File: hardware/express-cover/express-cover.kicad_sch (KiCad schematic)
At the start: 26 parts

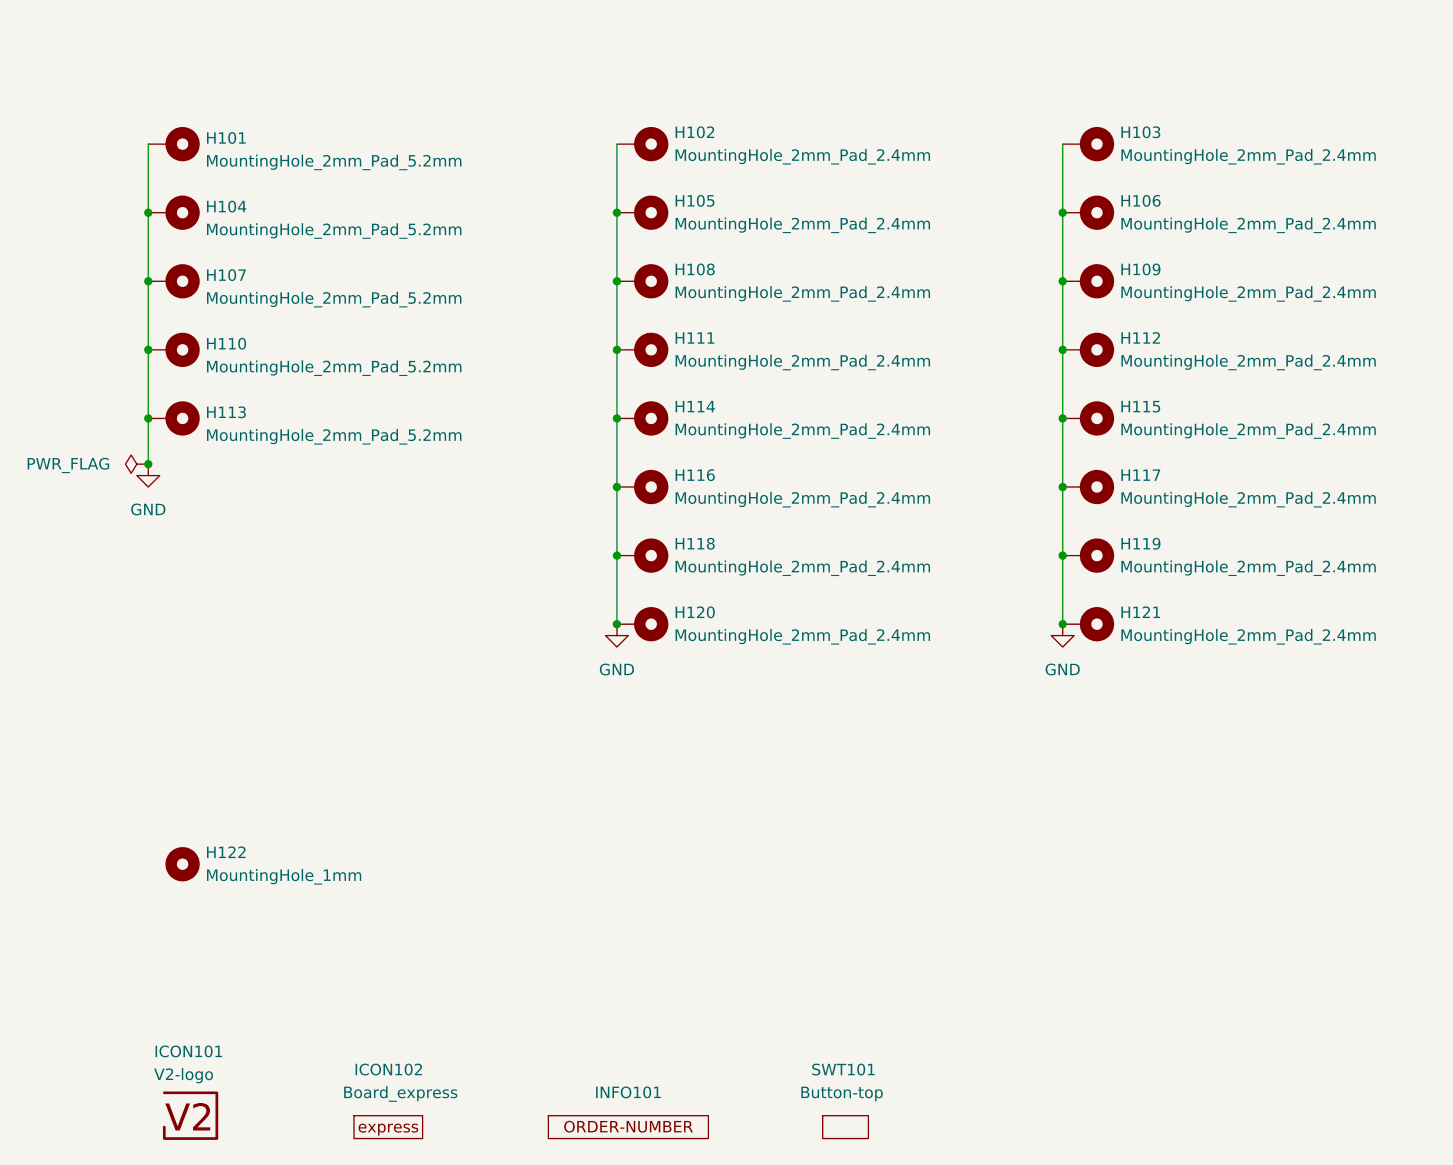
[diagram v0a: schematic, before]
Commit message: Replace Order_Number
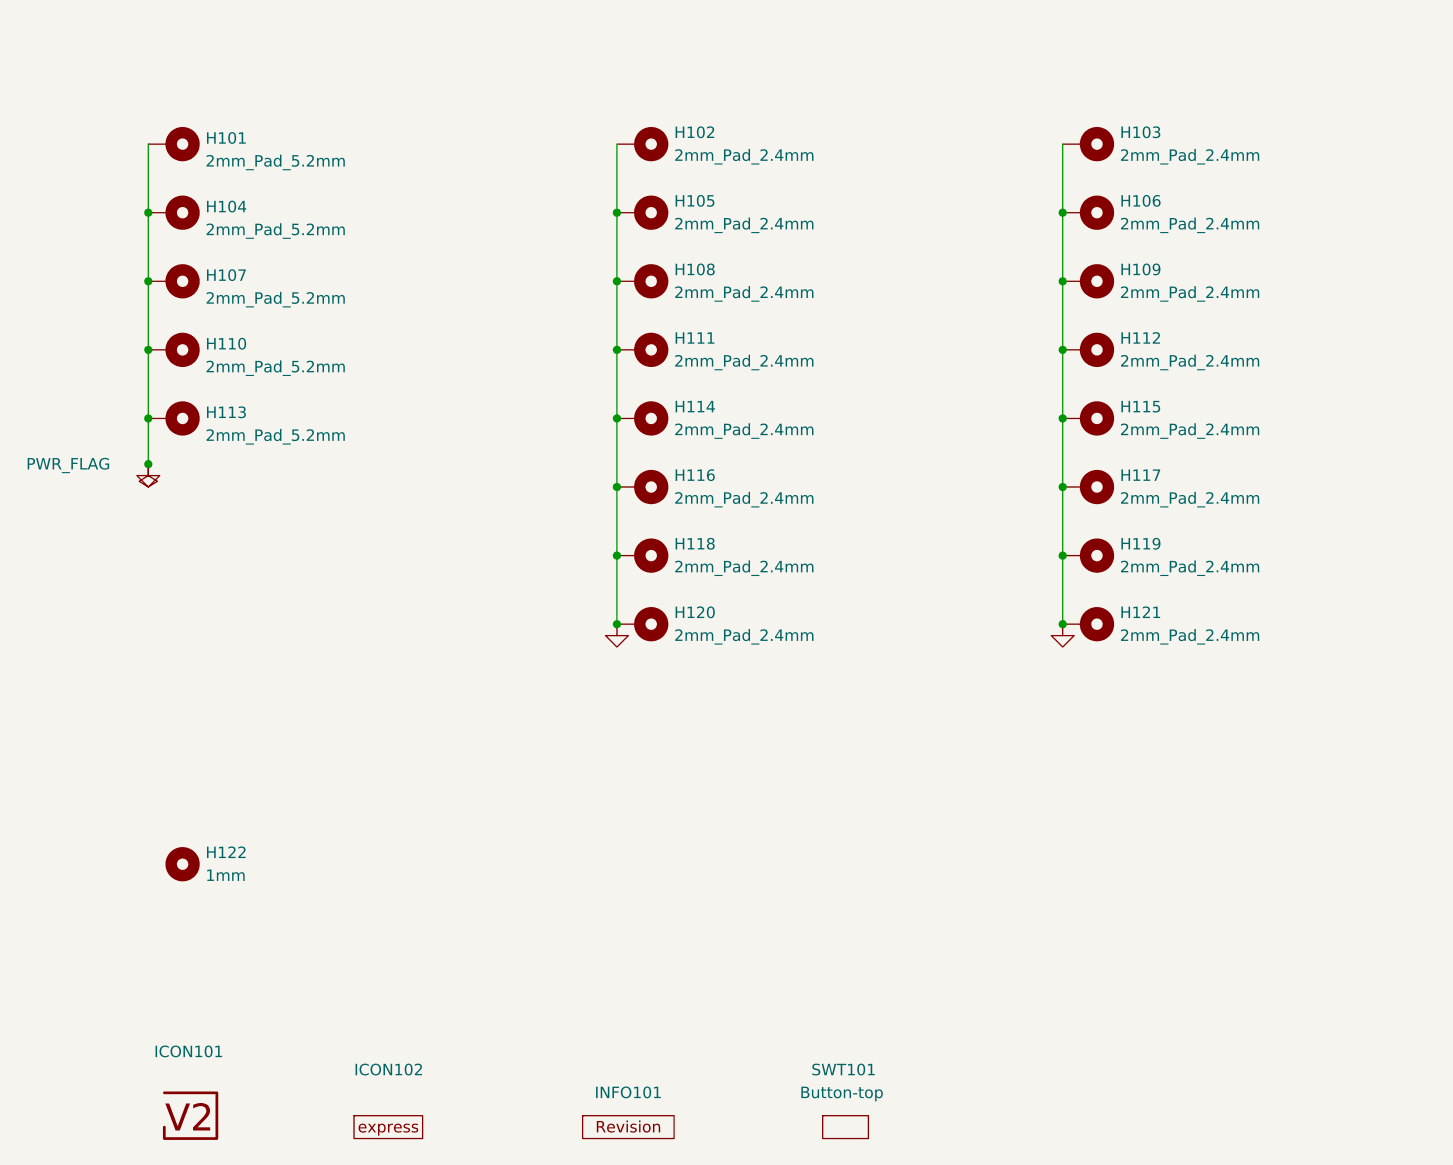
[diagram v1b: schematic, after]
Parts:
- H101, H104, H107, H110, H113: value MountingHole_2mm_Pad_5.2mm -> 2mm_Pad_5.2mm
- H102, H103, H105, H106, H108, H109, H111, H112, H114, H115, H116, H117, H118, H119, H120, H121: value MountingHole_2mm_Pad_2.4mm -> 2mm_Pad_2.4mm
- H122: value MountingHole_1mm -> 1mm
- INFO101: value Order_Number -> ~; footprint V2_Production:Order_Number -> V2_Production:Revision; symbol V2_Production:Order_Number -> V2_Production:Revision

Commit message: Update Library
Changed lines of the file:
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@@
-	)
-	(junction
-		(at 82.55 78.74)
-		(diameter 0)
-		(color 0 0 0 0)
 	)
 	(junction
@@
 		(dnp no)
 		(fields_autoplaced yes)
-		(property "Reference" "#PWR0103"
+		(property "Reference" "#PWR103"
 			(at 184.15 102.87 0)
 			(effects
@@
 			(project "express-cover"
 				(path "/6c8448b4-b04d-47e1-934e-e40cbe27a7be"
-					(reference "#PWR0103")
+					(reference "#PWR103")
 					(unit 1)
 				)
@@
 		(dnp no)
 		(fields_autoplaced yes)
-		(property "Reference" "#PWR0101"
+		(property "Reference" "#PWR101"
 			(at 82.55 85.09 0)
 			(effects
@@
 			(project "express-cover"
 				(path "/6c8448b4-b04d-47e1-934e-e40cbe27a7be"
-					(reference "#PWR0101")
+					(reference "#PWR101")
 					(unit 1)
 				)
@@
 	)
 	(symbol
+		(lib_id "V2_power:GND")
+		(at 86.36 30.48 90)
+		(unit 1)
+		(exclude_from_sim no)
+		(in_bom yes)
+		(on_board yes)
+		(dnp no)
+		(fields_autoplaced yes)
+		(property "Reference" "#PWR0104"
+			(at 92.71 30.48 0)
+			(effects
+				(font
+					(size 1.27 1.27)
+				)
+				(hide yes)
+			)
+		)
+		(property "Value" "GND"
+			(at 91.44 30.48 0)
+			(effects
+				(font
+					(size 1.27 1.27)
+				)
+				(hide yes)
+			)
+		)
+		(property "Footprint" ""
+			(at 86.36 30.48 0)
+			(effects
+				(font
+					(size 1.27 1.27)
+				)
+				(hide yes)
+			)
+		)
+		(property "Datasheet" ""
+			(at 86.36 30.48 0)
+			(effects
+				(font
+					(size 1.27 1.27)
+				)
+				(hide yes)
+			)
+		)
+		(property "Description" ""
+			(at 86.36 30.48 0)
+			(effects
+				(font
+					(size 1.27 1.27)
+				)
+				(hide yes)
+			)
+		)
+		(pin "1"
+		)
+		(instances
+			(project "express-cover"
+				(path "/6c8448b4-b04d-47e1-934e-e40cbe27a7be"
+					(reference "#PWR0104")
+					(unit 1)
+				)
+			)
+		)
+	)
+	(symbol
 		(lib_id "V2_Mechanical:MountingHole_2mm_Pad_2.4mm")
 		(at 137.16 43.18 270)
@@
 		(dnp no)
 		(fields_autoplaced yes)
-		(property "Reference" "#PWR0102"
+		(property "Reference" "#PWR102"
 			(at 134.62 102.87 0)
 			(effects
@@
 			(project "express-cover"
 				(path "/6c8448b4-b04d-47e1-934e-e40cbe27a7be"
-					(reference "#PWR0102")
+					(reference "#PWR102")
 					(unit 1)
 				)
@@
 	(symbol
 		(lib_id "V2_power:PWR_FLAG")
-		(at 82.55 78.74 90)
+		(at 86.36 30.48 0)
 		(unit 1)
 		(exclude_from_sim no)
@@
 		(on_board yes)
 		(dnp no)
-		(property "Reference" "#FLG0101"
-			(at 80.645 78.74 0)
+		(property "Reference" "#FLG101"
+			(at 86.36 28.575 0)
 			(effects
 				(font
@@
 		)
 		(property "Value" "PWR_FLAG"
-			(at 73.66 78.74 90)
+			(at 74.93 30.48 0)
 			(effects
 				(font
@@
 		)
 		(property "Footprint" ""
-			(at 82.55 78.74 0)
-			(effects
-				(font
-					(size 1.27 1.27)
-				)
-				(hide yes)
-			)
-		)
-		(property "Datasheet" ""
-			(at 82.55 78.74 0)
+			(at 86.36 30.48 0)
+			(effects
+				(font
+					(size 1.27 1.27)
+				)
+				(hide yes)
+			)
+		)
+		(property "Datasheet" ""
+			(at 86.36 30.48 0)
 			(effects
 				(font
@@
 		)
 		(property "Description" "Special symbol for telling ERC where power comes from"
-			(at 82.55 78.74 0)
-			(effects
-				(font
-					(size 1.27 1.27)
-				)
-				(hide yes)
-			)
-		)
-		(pin "1"
-		)
-		(instances
-			(project "express-cover"
-				(path "/6c8448b4-b04d-47e1-934e-e40cbe27a7be"
-					(reference "#FLG0101")
-					(unit 1)
-				)
+			(at 86.36 30.48 0)
+			(effects
+				(font
+					(size 1.27 1.27)
+				)
+				(hide yes)
+			)
+		)
+		(pin "1"
+		)
+		(instances
+			(project "express-cover"
+				(path "/6c8448b4-b04d-47e1-934e-e40cbe27a7be"
+					(reference "#FLG101")
+					(unit 1)
+				)
